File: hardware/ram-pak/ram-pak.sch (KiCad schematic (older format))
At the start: 15 parts, among them J1 PinHeader_2x22_P1.27mm, U1 TLV62568DBV

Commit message: Added missing 3d models.
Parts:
- J1: footprint pkl_pin_headers:PinHeader_2x22_P1.27mm_Vertical_Pass-Through__SMD -> pkl_pin_sockets:PinSocket_2x22_P1.27mm_Vertical_Pass-Through__SMD
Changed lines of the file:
@@
 F 0 "J1" H 6350 5667 50  0000 C CNN
 F 1 "PinHeader_2x22_P1.27mm" H 6350 5576 50  0000 C CNN
-F 2 "pkl_pin_headers:PinHeader_2x22_P1.27mm_Vertical_Pass-Through__SMD" H 6300 4450 50  0001 C CNN
+F 2 "pkl_pin_sockets:PinSocket_2x22_P1.27mm_Vertical_Pass-Through__SMD" H 6300 4450 50  0001 C CNN
 F 3 "~" H 6300 4450 50  0001 C CNN
 F 4 "conn-smd-005in-22-2-hdr" H 6300 4450 50  0001 C CNN "1b2-bom-key"

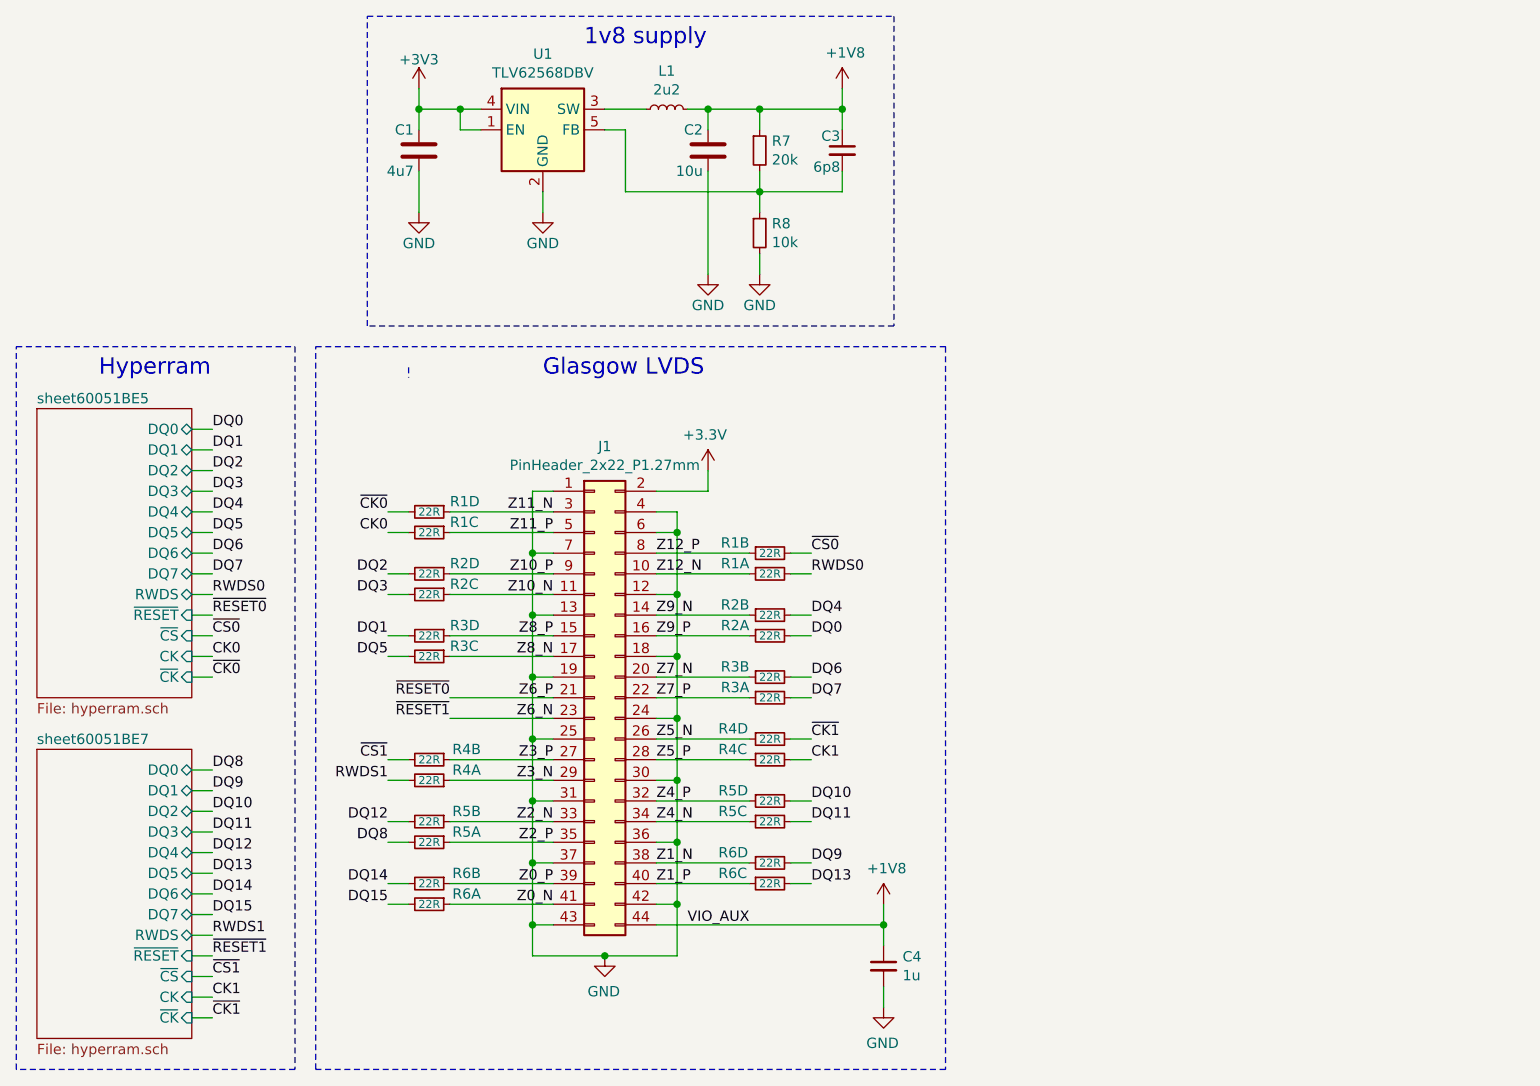
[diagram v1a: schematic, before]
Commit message: Ram-Pak: Routed and length matched.
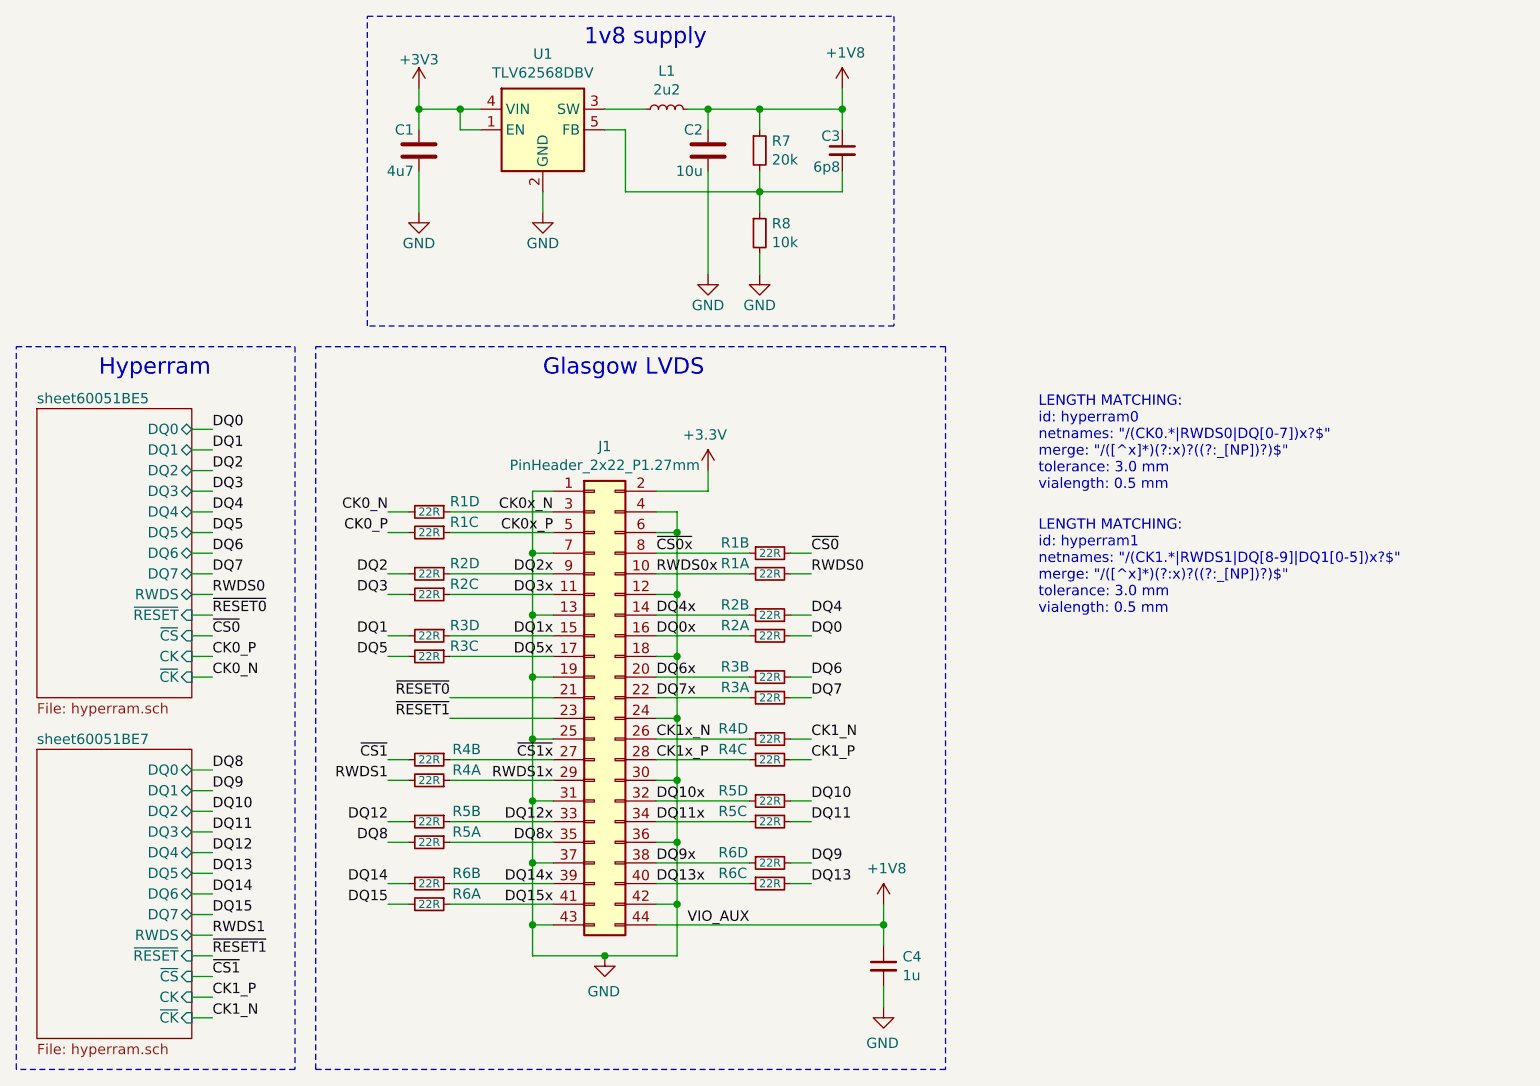
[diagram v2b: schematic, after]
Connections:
- net CK0 renamed CK0_P
- net CK1 renamed CK1_P
- net Z0_N renamed DQ15x
- net Z0_P renamed DQ14x
- net Z10_N renamed DQ3x
- net Z10_P renamed DQ2x
- net Z11_N renamed CK0x_N
- net Z11_P renamed CK0x_P
- net Z12_N renamed RWDS0x
- net Z12_P renamed ~CS0x
- net Z1_N renamed DQ9x
- net Z1_P renamed DQ13x
- net Z2_N renamed DQ12x
- net Z2_P renamed DQ8x
- net Z3_N renamed RWDS1x
- net Z3_P renamed ~CS1x
- net Z4_N renamed DQ11x
- net Z4_P renamed DQ10x
- net Z5_N renamed CK1x_N
- net Z5_P renamed CK1x_P
- net Z6_N renamed ~RESET1
- net Z6_P renamed ~RESET0
- net Z7_N renamed DQ6x
- net Z7_P renamed DQ7x
- net Z8_N renamed DQ5x
- net Z8_P renamed DQ1x
- net Z9_N renamed DQ4x
- net Z9_P renamed DQ0x
- net ~CK0 renamed CK0_N
- net ~CK1 renamed CK1_N
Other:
- note added: "LENGTH MATCHING:\nid: hyperram0\nnetnames: "/(CK0.*|RWDS0|DQ[0-7])x?$"\nmerge: "/([^x]*)(?:x)?((?:_[NP])?)$"\ntolerance: 3.0 mm\nvialength: 0.5 mm"
- note added: "LENGTH MATCHING:\nid: hyperram1\nnetnames: "/(CK1.*|RWDS1|DQ[8-9]|DQ1[0-5])x?$"\nmerge: "/([^x]*)(?:x)?((?:_[NP])?)$"\ntolerance: 3.0 mm\nvialength: 0.5 mm"
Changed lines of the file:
@@
 $EndDescr
 Text Label 6100 3650 2    50   ~ 0
-Z11_P
+CK0x_P
 Wire Wire Line
 	6100 3450 6000 3450
@@
 VIO_AUX
 Text Label 6600 3750 0    50   ~ 0
-Z12_P
-Text Label 6600 3850 0    50   ~ 0
-Z12_N
-Text Label 6600 4050 0    50   ~ 0
-Z9_N
-Text Label 6600 4150 0    50   ~ 0
-Z9_P
-Text Label 6600 4350 0    50   ~ 0
-Z7_N
-Text Label 6600 4450 0    50   ~ 0
-Z7_P
-Text Label 6600 4650 0    50   ~ 0
-Z5_N
-Text Label 6600 4750 0    50   ~ 0
-Z5_P
-Text Label 6600 4950 0    50   ~ 0
-Z4_P
-Text Label 6600 5050 0    50   ~ 0
-Z4_N
-Text Label 6600 5250 0    50   ~ 0
-Z1_N
-Text Label 6600 5350 0    50   ~ 0
-Z1_P
-Text Label 6100 5450 2    50   ~ 0
-Z0_N
-Text Label 6100 5350 2    50   ~ 0
-Z0_P
-Text Label 6100 5150 2    50   ~ 0
-Z2_P
-Text Label 6100 5050 2    50   ~ 0
-Z2_N
-Text Label 6100 4850 2    50   ~ 0
-Z3_N
-Text Label 6100 4750 2    50   ~ 0
-Z3_P
-Text Label 6100 4550 2    50   ~ 0
-Z6_N
-Text Label 6100 4450 2    50   ~ 0
-Z6_P
-Text Label 6100 4250 2    50   ~ 0
-Z8_N
-Text Label 6100 4150 2    50   ~ 0
-Z8_P
-Text Label 6100 3950 2    50   ~ 0
-Z10_N
+~CS0x
 Text Label 6100 3850 2    50   ~ 0
-Z10_P
+DQ2x
 Text Label 6100 3550 2    50   ~ 0
-Z11_N
+CK0x_N
 Wire Wire Line
 	6600 3650 6700 3650
@@
 Wire Wire Line
 	6600 4050 7050 4050
-Wire Wire Line
-	7050 3850 6600 3850
 Wire Wire Line
 	6600 3750 7050 3750
@@
 Text Label 7350 4050 0    50   ~ 0
 DQ4
-Text Label 5300 4250 2    50   ~ 0
-DQ5
 Text Label 7350 4350 0    50   ~ 0
 DQ6
@@
 ~CS0
 Text Label 4450 4250 0    50   ~ 0
-CK0
+CK0_P
 Text Label 4450 4350 0    50   ~ 0
-~CK0
+CK0_N
 $Sheet
 S 3600 4700 750  1400
@@
 ~CS1
 Text Label 4450 5900 0    50   ~ 0
-CK1
+CK1_P
 Text Label 4450 6000 0    50   ~ 0
-~CK1
+CK1_N
 Wire Notes Line
 	7750 2650 5200 2650
@@
 ~CS0
 Text Label 5300 3650 2    50   ~ 0
-CK0
+CK0_P
 Text Label 5300 3550 2    50   ~ 0
-~CK0
+CK0_N
 Text Label 5300 4850 2    50   ~ 0
 RWDS1
@@
 ~CS1
 Text Label 7350 4750 0    50   ~ 0
-CK1
+CK1_P
 Text Label 7350 4650 0    50   ~ 0
-~CK1
+CK1_N
 Text Label 5600 4550 2    50   ~ 0
 ~RESET1
@@
 Text Notes 6050 2900 0    79   ~ 0
 Glasgow LVDS
-Wire Notes Line
-	5400 2850 5400 2900
 Text Notes 3900 2900 0    79   ~ 0
 Hyperram
+Text Notes 8450 3450 0    50   ~ 0
+LENGTH MATCHING:\nid: hyperram0\nnetnames: "/(CK0.*|RWDS0|DQ[0-7])x?$"\nmerge: "/([^x]*)(?:x)?((?:_[NP])?)$"\ntolerance: 3.0 mm\nvialength: 0.5 mm
+Text Notes 8450 4050 0    50   ~ 0
+LENGTH MATCHING:\nid: hyperram1\nnetnames: "/(CK1.*|RWDS1|DQ[8-9]|DQ1[0-5])x?$"\nmerge: "/([^x]*)(?:x)?((?:_[NP])?)$"\ntolerance: 3.0 mm\nvialength: 0.5 mm
+Wire Wire Line
+	7050 3850 6600 3850
+Text Label 6100 3950 2    50   ~ 0
+DQ3x
+Text Label 6600 3850 0    50   ~ 0
+RWDS0x
+Text Label 6600 4050 0    50   ~ 0
+DQ4x
+Text Label 6600 4150 0    50   ~ 0
+DQ0x
+Text Label 6600 4350 0    50   ~ 0
+DQ6x
+Text Label 6600 4450 0    50   ~ 0
+DQ7x
+Text Label 6600 4650 0    50   ~ 0
+CK1x_N
+Text Label 6600 4750 0    50   ~ 0
+CK1x_P
+Text Label 6600 4950 0    50   ~ 0
+DQ10x
+Text Label 6600 5050 0    50   ~ 0
+DQ11x
+Text Label 6600 5250 0    50   ~ 0
+DQ9x
+Text Label 6600 5350 0    50   ~ 0
+DQ13x
+Text Label 6100 5350 2    50   ~ 0
+DQ14x
+Text Label 6100 5450 2    50   ~ 0
+DQ15x
+Text Label 6100 5150 2    50   ~ 0
+DQ8x
+Text Label 6100 5050 2    50   ~ 0
+DQ12x
+Text Label 6100 4850 2    50   ~ 0
+RWDS1x
+Text Label 6100 4750 2    50   ~ 0
+~CS1x
+Text Label 6100 4150 2    50   ~ 0
+DQ1x
+Text Label 5300 4250 2    50   ~ 0
+DQ5
+Text Label 6100 4250 2    50   ~ 0
+DQ5x
 $EndSCHEMATC

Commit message: ram-pak: Extended and updated BOM information.
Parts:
- C1: 1b2-bom-key (none) -> cap-cer-0603-4u7; Key cap-cer-0603-4u7 -> (none)
- C2: 1b2-bom-key (none) -> cap-cer-0603-10u; Key cap-cer-0603-4u7 -> (none)
- C3: 1b2-bom-key (none) -> cap-cer-0402-6p8; Key cap-cer-0402-470p -> (none)
- C4: 1b2-bom-key (none) -> cap-cer-0402-1u
- L1: 1b2-bom-key (none) -> ind-0805-2u2
- R1, R2, R3, R4, R5, R6: 1b2-bom-key (none) -> res-0402cv-array-4-22
- R7: 1b2-bom-key (none) -> res-0402-20k
- R8: 1b2-bom-key (none) -> res-0402-10k
- U1: 1b2-bom-key (none) -> vreg-tlv62568
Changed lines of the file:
@@
 F 2 "pkl_dipol:R_Array_Convex_4x0402" H 7209 3759 60  0001 L CNN
 F 3 "" H 7150 3850 60  0001 C CNN
+F 4 "res-0402cv-array-4-22" H 7150 3850 50  0001 C CNN "1b2-bom-key"
 	1    7150 3850
 	0    -1   1    0
@@
 F 2 "pkl_dipol:C_0402" H 7792 5659 60  0001 L CNN
 F 3 "" H 7700 5750 60  0001 C CNN
+F 4 "cap-cer-0402-1u" H 7700 5750 50  0001 C CNN "1b2-bom-key"
 	1    7700 5750
 	1    0    0    -1
@@
 F 2 "pkl_dipol:R_Array_Convex_4x0402" H 5559 3559 60  0001 L CNN
 F 3 "" H 5500 3650 60  0001 C CNN
+F 4 "res-0402cv-array-4-22" H 5500 3650 50  0001 C CNN "1b2-bom-key"
 	3    5500 3650
 	0    1    1    0
@@
 F 2 "pkl_dipol:R_Array_Convex_4x0402" H 5559 3459 60  0001 L CNN
 F 3 "" H 5500 3550 60  0001 C CNN
+F 4 "res-0402cv-array-4-22" H 5500 3550 50  0001 C CNN "1b2-bom-key"
 	4    5500 3550
 	0    1    1    0
@@
 F 2 "pkl_dipol:R_Array_Convex_4x0402" H 7209 4059 60  0001 L CNN
 F 3 "" H 7150 4150 60  0001 C CNN
+F 4 "res-0402cv-array-4-22" H 7150 4150 50  0001 C CNN "1b2-bom-key"
 	1    7150 4150
 	0    -1   1    0
@@
 F 2 "pkl_dipol:R_Array_Convex_4x0402" H 7209 3959 60  0001 L CNN
 F 3 "" H 7150 4050 60  0001 C CNN
+F 4 "res-0402cv-array-4-22" H 7150 4050 50  0001 C CNN "1b2-bom-key"
 	2    7150 4050
 	0    -1   1    0
@@
 F 2 "pkl_dipol:R_Array_Convex_4x0402" H 5559 3859 60  0001 L CNN
 F 3 "" H 5500 3950 60  0001 C CNN
+F 4 "res-0402cv-array-4-22" H 5500 3950 50  0001 C CNN "1b2-bom-key"
 	3    5500 3950
 	0    1    1    0
@@
 F 2 "pkl_dipol:R_Array_Convex_4x0402" H 5559 3759 60  0001 L CNN
 F 3 "" H 5500 3850 60  0001 C CNN
+F 4 "res-0402cv-array-4-22" H 5500 3850 50  0001 C CNN "1b2-bom-key"
 	4    5500 3850
 	0    1    1    0
@@
 F 2 "pkl_dipol:R_Array_Convex_4x0402" H 7209 4359 60  0001 L CNN
 F 3 "" H 7150 4450 60  0001 C CNN
+F 4 "res-0402cv-array-4-22" H 7150 4450 50  0001 C CNN "1b2-bom-key"
 	1    7150 4450
 	0    -1   1    0
@@
 F 2 "pkl_dipol:R_Array_Convex_4x0402" H 7209 4259 60  0001 L CNN
 F 3 "" H 7150 4350 60  0001 C CNN
+F 4 "res-0402cv-array-4-22" H 7150 4350 50  0001 C CNN "1b2-bom-key"
 	2    7150 4350
 	0    -1   1    0
@@
 F 2 "pkl_dipol:R_Array_Convex_4x0402" H 5559 4159 60  0001 L CNN
 F 3 "" H 5500 4250 60  0001 C CNN
+F 4 "res-0402cv-array-4-22" H 5500 4250 50  0001 C CNN "1b2-bom-key"
 	3    5500 4250
 	0    1    1    0
@@
 F 2 "pkl_dipol:R_Array_Convex_4x0402" H 5559 4059 60  0001 L CNN
 F 3 "" H 5500 4150 60  0001 C CNN
+F 4 "res-0402cv-array-4-22" H 5500 4150 50  0001 C CNN "1b2-bom-key"
 	4    5500 4150
 	0    1    1    0
@@
 F 2 "pkl_dipol:R_Array_Convex_4x0402" H 5559 4759 60  0001 L CNN
 F 3 "" H 5500 4850 60  0001 C CNN
+F 4 "res-0402cv-array-4-22" H 5500 4850 50  0001 C CNN "1b2-bom-key"
 	1    5500 4850
 	0    1    -1   0
@@
 F 2 "pkl_dipol:R_Array_Convex_4x0402" H 5559 4659 60  0001 L CNN
 F 3 "" H 5500 4750 60  0001 C CNN
+F 4 "res-0402cv-array-4-22" H 5500 4750 50  0001 C CNN "1b2-bom-key"
 	2    5500 4750
 	0    1    1    0
@@
 F 2 "pkl_dipol:R_Array_Convex_4x0402" H 7209 4659 60  0001 L CNN
 F 3 "" H 7150 4750 60  0001 C CNN
+F 4 "res-0402cv-array-4-22" H 7150 4750 50  0001 C CNN "1b2-bom-key"
 	3    7150 4750
 	0    -1   1    0
@@
 F 2 "pkl_dipol:R_Array_Convex_4x0402" H 7209 4559 60  0001 L CNN
 F 3 "" H 7150 4650 60  0001 C CNN
+F 4 "res-0402cv-array-4-22" H 7150 4650 50  0001 C CNN "1b2-bom-key"
 	4    7150 4650
 	0    -1   1    0
@@
 F 2 "pkl_dipol:R_Array_Convex_4x0402" H 5559 5059 60  0001 L CNN
 F 3 "" H 5500 5150 60  0001 C CNN
+F 4 "res-0402cv-array-4-22" H 5500 5150 50  0001 C CNN "1b2-bom-key"
 	1    5500 5150
 	0    1    1    0
@@
 F 2 "pkl_dipol:R_Array_Convex_4x0402" H 5559 4959 60  0001 L CNN
 F 3 "" H 5500 5050 60  0001 C CNN
+F 4 "res-0402cv-array-4-22" H 5500 5050 50  0001 C CNN "1b2-bom-key"
 	2    5500 5050
 	0    1    1    0
@@
 F 2 "pkl_dipol:R_Array_Convex_4x0402" H 5559 5359 60  0001 L CNN
 F 3 "" H 5500 5450 60  0001 C CNN
+F 4 "res-0402cv-array-4-22" H 5500 5450 50  0001 C CNN "1b2-bom-key"
 	1    5500 5450
 	0    1    1    0
@@
 F 2 "pkl_dipol:R_Array_Convex_4x0402" H 5559 5259 60  0001 L CNN
 F 3 "" H 5500 5350 60  0001 C CNN
+F 4 "res-0402cv-array-4-22" H 5500 5350 50  0001 C CNN "1b2-bom-key"
 	2    5500 5350
 	0    1    1    0
@@
 F 2 "pkl_dipol:R_Array_Convex_4x0402" H 7209 5259 60  0001 L CNN
 F 3 "" H 7150 5350 60  0001 C CNN
+F 4 "res-0402cv-array-4-22" H 7150 5350 50  0001 C CNN "1b2-bom-key"
 	3    7150 5350
 	0    -1   1    0
@@
 F 2 "pkl_dipol:R_Array_Convex_4x0402" H 7209 5159 60  0001 L CNN
 F 3 "" H 7150 5250 60  0001 C CNN
+F 4 "res-0402cv-array-4-22" H 7150 5250 50  0001 C CNN "1b2-bom-key"
 	4    7150 5250
 	0    -1   1    0
@@
 F 2 "pkl_dipol:R_Array_Convex_4x0402" H 7209 4959 60  0001 L CNN
 F 3 "" H 7150 5050 60  0001 C CNN
+F 4 "res-0402cv-array-4-22" H 7150 5050 50  0001 C CNN "1b2-bom-key"
 	3    7150 5050
 	0    -1   1    0
@@
 F 2 "pkl_dipol:R_Array_Convex_4x0402" H 7209 4859 60  0001 L CNN
 F 3 "" H 7150 4950 60  0001 C CNN
+F 4 "res-0402cv-array-4-22" H 7150 4950 50  0001 C CNN "1b2-bom-key"
 	4    7150 4950
 	0    -1   1    0
@@
 F 2 "pkl_housings_sot:SOT-23-5" H 6100 1450 50  0001 L CIN
 F 3 "http://www.ti.com/lit/ds/symlink/tlv62568.pdf" H 5800 2150 50  0001 C CNN
+F 4 "vreg-tlv62568" H 6050 1700 50  0001 C CNN "1b2-bom-key"
 	1    6050 1700
 	1    0    0    -1
@@
 F 2 "pkl_dipol:C_0603" H 5488 1650 30  0001 C CNN
 F 3 "" H 5450 1800 60  0000 C CNN
-F 4 "cap-cer-0603-4u7" H 5450 1800 60  0001 C CNN "Key"
+F 4 "cap-cer-0603-4u7" H 5450 1800 60  0001 C CNN "1b2-bom-key"
 F 5 "0603" H 5450 1800 60  0001 C CNN "Package ID"
 F 6 "ANY" H 5450 1800 60  0001 C CNN "Source"
@@
 F 2 "pkl_dipol:L_0805" V 6650 1600 60  0001 C CNN
 F 3 "" V 6650 1600 60  0001 C CNN
+F 4 "ind-0805-2u2" H 6650 1600 50  0001 C CNN "1b2-bom-key"
 	1    6650 1600
 	0    -1   -1   0
@@
 F 2 "pkl_dipol:C_0603" H 6888 1650 30  0001 C CNN
 F 3 "" H 6850 1800 60  0000 C CNN
-F 4 "cap-cer-0603-4u7" H 6850 1800 60  0001 C CNN "Key"
+F 4 "cap-cer-0603-10u" H 6850 1800 60  0001 C CNN "1b2-bom-key"
 F 5 "0603" H 6850 1800 60  0001 C CNN "Package ID"
 F 6 "ANY" H 6850 1800 60  0001 C CNN "Source"
@@
 F 2 "pkl_dipol:R_0402" H 7159 1709 60  0001 L CNN
 F 3 "" H 7100 1800 60  0001 C CNN
+F 4 "res-0402-20k" H 7100 1800 50  0001 C CNN "1b2-bom-key"
 	1    7100 1800
 	1    0    0    -1
@@
 F 2 "pkl_dipol:R_0402" H 7100 2200 60  0001 C CNN
 F 3 "" H 7100 2200 60  0001 C CNN
+F 4 "res-0402-10k" H 7100 2200 50  0001 C CNN "1b2-bom-key"
 	1    7100 2200
 	1    0    0    -1
@@
 F 2 "pkl_dipol:C_0402" H 7500 1800 60  0001 C CNN
 F 3 "" H 7500 1800 60  0000 C CNN
-F 4 "cap-cer-0402-470p" H 7500 1800 60  0001 C CNN "Key"
+F 4 "cap-cer-0402-6p8" H 7500 1800 60  0001 C CNN "1b2-bom-key"
 F 5 "0402" H 7500 1800 60  0001 C CNN "Package ID"
 F 6 "ANY" H 7500 1800 60  0001 C CNN "Source"
@@
 F 2 "pkl_dipol:R_Array_Convex_4x0402" H 7209 3659 60  0001 L CNN
 F 3 "" H 7150 3750 60  0001 C CNN
+F 4 "res-0402cv-array-4-22" H 7150 3750 50  0001 C CNN "1b2-bom-key"
 	2    7150 3750
 	0    -1   1    0

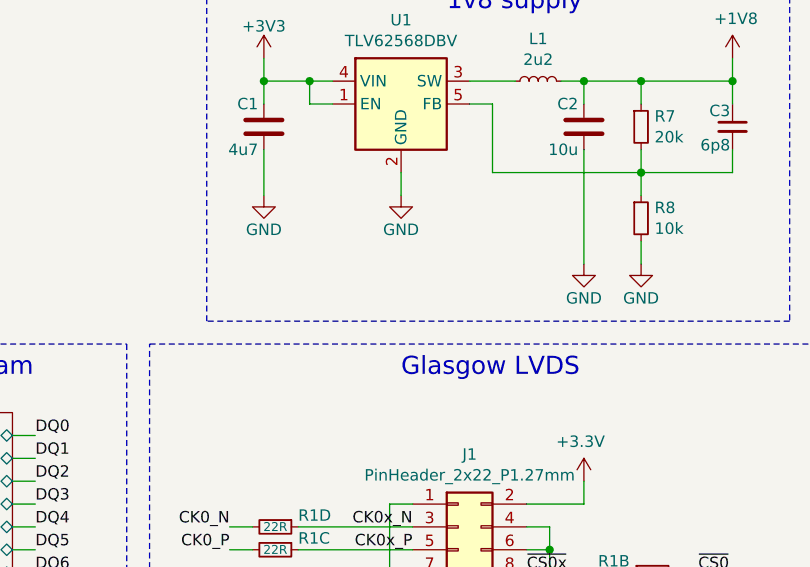
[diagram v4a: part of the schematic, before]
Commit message: ram-pak: Removed back pads, added VSKIP bumped version.
* Removed the back side connector mounting pads. (only needed for the
  first prototype using 1.6mm thick pcb)
* Added VSKIP that allows the use of 3v3 RAM chips.
* Bumped version to V0.1b
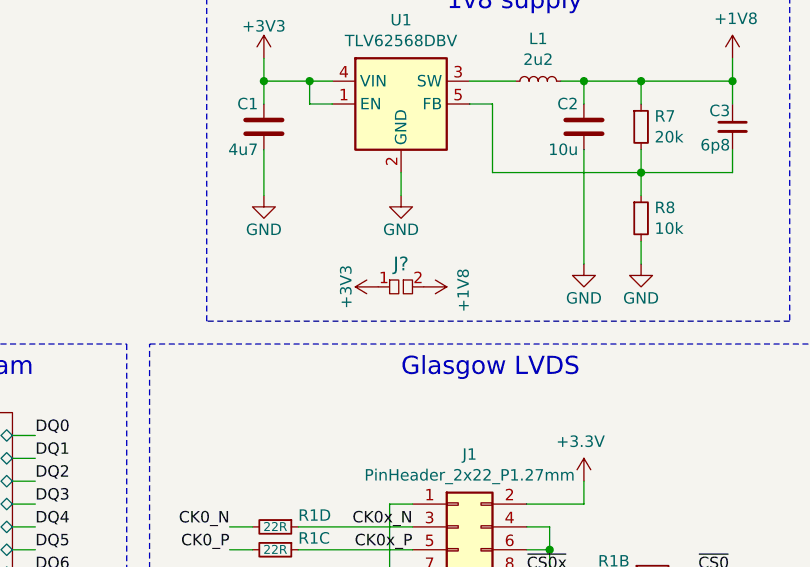
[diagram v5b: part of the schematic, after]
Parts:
- added J?: pkl_jumper, pkl_jumpers:J_0603, symbol pkl_misc:pkl_jumper
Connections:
- net +1V8: now also J?.2
- net +3V3: now also J?.1
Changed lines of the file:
@@
 Title "Glasgow Ram-Pak"
 Date ""
-Rev "V0.1a"
+Rev "V0.1b"
 Comp "1BitSquared"
 Comment1 "(C) 2021 1BitSquared"
@@
 Text Label 6100 4250 2    50   ~ 0
 DQ5x
+$Comp
+L pkl_misc:pkl_jumper J?
+U 1 1 602E83F4
+P 6050 2500
+F 0 "J?" H 6050 2600 60  0000 C CNN
+F 1 "pkl_jumper" H 6050 2641 60  0001 C CNN
+F 2 "pkl_jumpers:J_0603" H 6050 2500 60  0001 C CNN
+F 3 "" H 6050 2500 60  0001 C CNN
+	1    6050 2500
+	1    0    0    -1
+$EndComp
+$Comp
+L power:+3V3 #PWR?
+U 1 1 602E9589
+P 5950 2500
+F 0 "#PWR?" H 5950 2350 50  0001 C CNN
+F 1 "+3V3" H 5950 2640 50  0000 C CNN
+F 2 "" H 5950 2500 60  0000 C CNN
+F 3 "" H 5950 2500 60  0000 C CNN
+F 4 "ANY" H 5950 2500 50  0001 C CNN "Source"
+	1    5950 2500
+	0    -1   -1   0
+$EndComp
+$Comp
+L power:+1V8 #PWR?
+U 1 1 602EA3A9
+P 6150 2500
+F 0 "#PWR?" H 6150 2350 50  0001 C CNN
+F 1 "+1V8" H 6165 2673 50  0000 C CNN
+F 2 "" H 6150 2500 50  0001 C CNN
+F 3 "" H 6150 2500 50  0001 C CNN
+	1    6150 2500
+	0    1    1    0
+$EndComp
 $EndSCHEMATC
